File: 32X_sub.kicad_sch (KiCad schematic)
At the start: 105 parts, among them IC511 315-5684, IC512 315-5788, IC515 74HC74, IC516 74LS00, T520 TestPoint, T526 TestPoint, T527 TestPoint, T528 TestPoint, T547 TestPoint, T548 TestPoint, T555 TestPoint, T599 AS, X501 *3

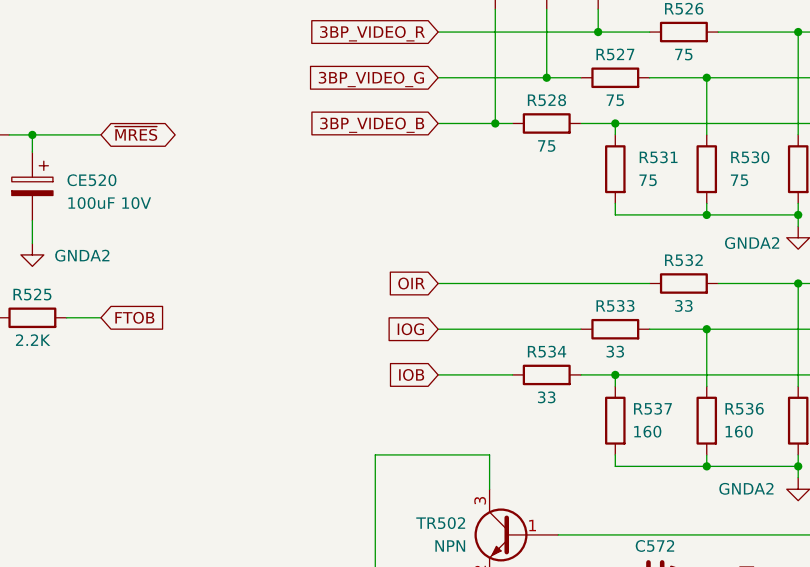
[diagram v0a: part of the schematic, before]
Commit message: Rename OIR -> IOR (issue #20).
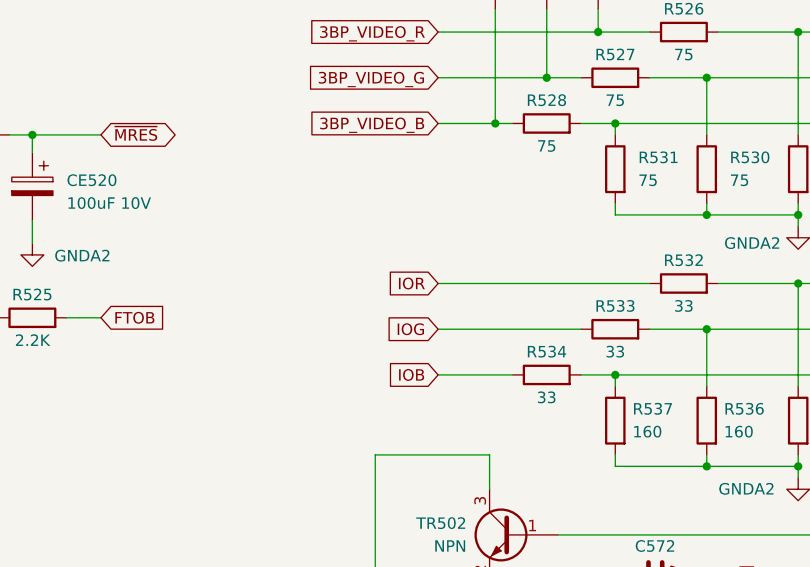
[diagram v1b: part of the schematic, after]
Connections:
- net OIR renamed IOR
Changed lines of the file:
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@@
 		)
 	)
-	(global_label "OIR"
+	(global_label "IOR"
 		(shape input)
 		(at 240.665 60.96 180)
